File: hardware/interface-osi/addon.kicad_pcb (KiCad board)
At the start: 2 copper layers, 43.2 x 54 mm, 22 parts, among them J1 Conn_01x16, U1 4066, U2 74LS14

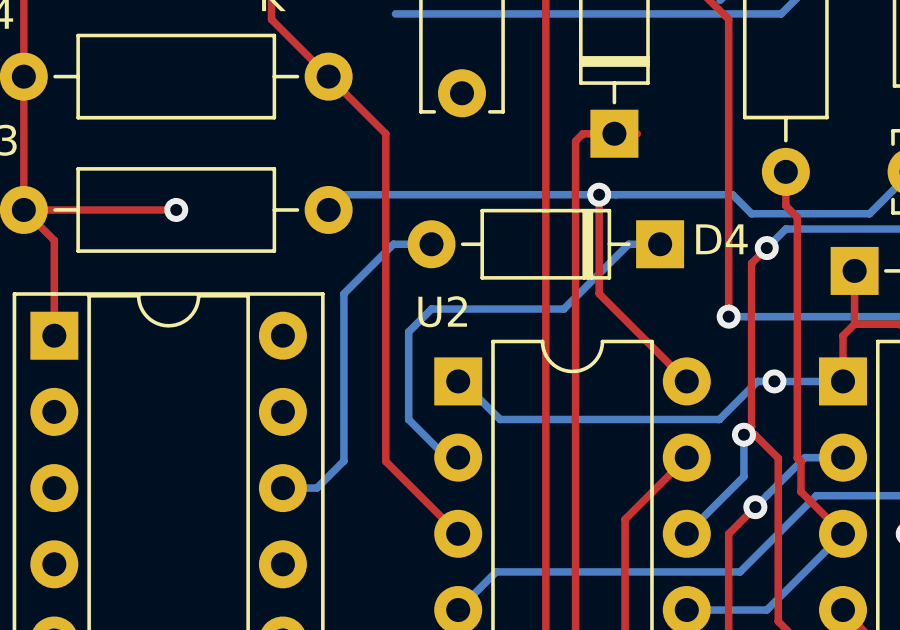
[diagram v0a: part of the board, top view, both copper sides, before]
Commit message: addon board uses 74HC14
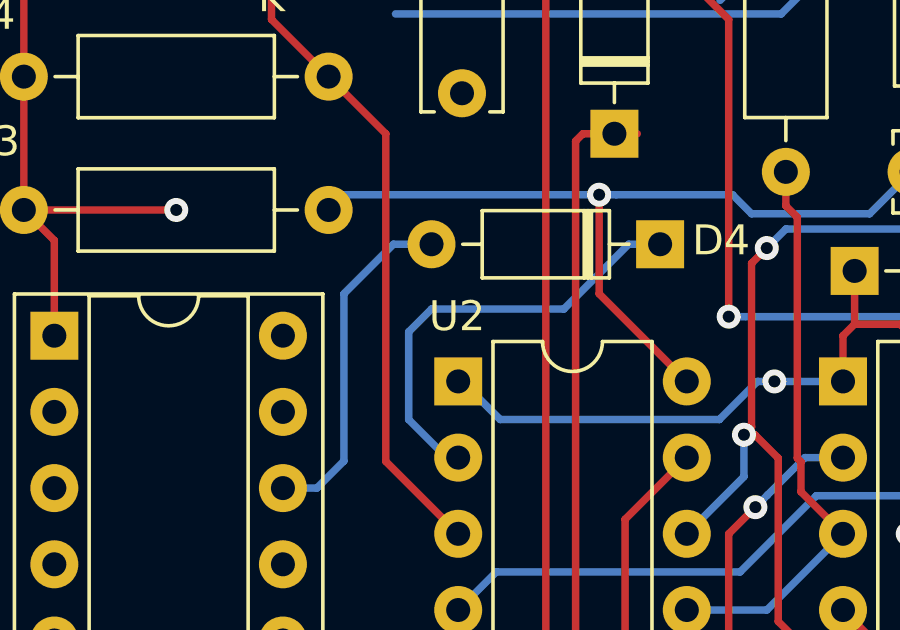
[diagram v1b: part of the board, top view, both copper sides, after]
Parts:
- R5: value 22k -> 10k
- R6: value 220k -> 100k
- U2: value 74LS14 -> 74HC14
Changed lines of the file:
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@@
     (add_net ~RESET)
+  )
+  (module Package_DIP:DIP-14_W7.62mm (layer F.Cu)
+    (at 124.333 62.865)
+    (descr "14-lead though-hole mounted DIP package, row spacing 7.62 mm (300 mils)")
+    (tags "THT DIP DIL PDIP 2.54mm 7.62mm 300mil")
+    (fp_text reference U2 (at -0.0381 -2.1717) (layer F.SilkS)
+      (effects (font (size 1 1) (thickness 0.15)))
+    )
+    (fp_text value 74HC14 (at 3.81 17.57) (layer F.Fab)
+      (effects (font (size 1 1) (thickness 0.15)))
+    )
+    (fp_text user %R (at 3.81 7.62) (layer F.Fab)
+      (effects (font (size 1 1) (thickness 0.15)))
+    )
+    (fp_line (start 8.7 -1.55) (end -1.1 -1.55) (layer F.CrtYd) (width 0.05))
+    (fp_line (start 8.7 16.8) (end 8.7 -1.55) (layer F.CrtYd) (width 0.05))
+    (fp_line (start -1.1 16.8) (end 8.7 16.8) (layer F.CrtYd) (width 0.05))
+    (fp_line (start -1.1 -1.55) (end -1.1 16.8) (layer F.CrtYd) (width 0.05))
+    (fp_line (start 6.46 -1.33) (end 4.81 -1.33) (layer F.SilkS) (width 0.12))
+    (fp_line (start 6.46 16.57) (end 6.46 -1.33) (layer F.SilkS) (width 0.12))
+    (fp_line (start 1.16 16.57) (end 6.46 16.57) (layer F.SilkS) (width 0.12))
+    (fp_line (start 1.16 -1.33) (end 1.16 16.57) (layer F.SilkS) (width 0.12))
+    (fp_line (start 2.81 -1.33) (end 1.16 -1.33) (layer F.SilkS) (width 0.12))
+    (fp_line (start 0.635 -0.27) (end 1.635 -1.27) (layer F.Fab) (width 0.1))
+    (fp_line (start 0.635 16.51) (end 0.635 -0.27) (layer F.Fab) (width 0.1))
+    (fp_line (start 6.985 16.51) (end 0.635 16.51) (layer F.Fab) (width 0.1))
+    (fp_line (start 6.985 -1.27) (end 6.985 16.51) (layer F.Fab) (width 0.1))
+    (fp_line (start 1.635 -1.27) (end 6.985 -1.27) (layer F.Fab) (width 0.1))
+    (fp_arc (start 3.81 -1.33) (end 2.81 -1.33) (angle -180) (layer F.SilkS) (width 0.12))
+    (pad 14 thru_hole oval (at 7.62 0) (size 1.6 1.6) (drill 0.8) (layers *.Cu *.Mask)
+      (net 7 ShifLockLED+))
+    (pad 7 thru_hole oval (at 0 15.24) (size 1.6 1.6) (drill 0.8) (layers *.Cu *.Mask)
+      (net 1 GND))
+    (pad 13 thru_hole oval (at 7.62 2.54) (size 1.6 1.6) (drill 0.8) (layers *.Cu *.Mask)
+      (net 14 "Net-(C1-Pad2)"))
+    (pad 6 thru_hole oval (at 0 12.7) (size 1.6 1.6) (drill 0.8) (layers *.Cu *.Mask)
+      (net 19 "Net-(R7-Pad2)"))
+    (pad 12 thru_hole oval (at 7.62 5.08) (size 1.6 1.6) (drill 0.8) (layers *.Cu *.Mask)
+      (net 4 "Net-(JP1-Pad3)"))
+    (pad 5 thru_hole oval (at 0 10.16) (size 1.6 1.6) (drill 0.8) (layers *.Cu *.Mask)
+      (net 26 "Net-(U1-Pad13)"))
+    (pad 11 thru_hole oval (at 7.62 7.62) (size 1.6 1.6) (drill 0.8) (layers *.Cu *.Mask)
+      (net 18 "Net-(R5-Pad1)"))
+    (pad 4 thru_hole oval (at 0 7.62) (size 1.6 1.6) (drill 0.8) (layers *.Cu *.Mask)
+      (net 26 "Net-(U1-Pad13)"))
+    (pad 10 thru_hole oval (at 7.62 10.16) (size 1.6 1.6) (drill 0.8) (layers *.Cu *.Mask)
+      (net 24 "Net-(JP1-Pad1)"))
+    (pad 3 thru_hole oval (at 0 5.08) (size 1.6 1.6) (drill 0.8) (layers *.Cu *.Mask)
+      (net 15 "Net-(C2-Pad1)"))
+    (pad 9 thru_hole oval (at 7.62 12.7) (size 1.6 1.6) (drill 0.8) (layers *.Cu *.Mask)
+      (net 24 "Net-(JP1-Pad1)"))
+    (pad 2 thru_hole oval (at 0 2.54) (size 1.6 1.6) (drill 0.8) (layers *.Cu *.Mask)
+      (net 27 "Net-(D4-Pad1)"))
+    (pad 8 thru_hole oval (at 7.62 15.24) (size 1.6 1.6) (drill 0.8) (layers *.Cu *.Mask)
+      (net 25 "Net-(R5-Pad2)"))
+    (pad 1 thru_hole rect (at 0 0) (size 1.6 1.6) (drill 0.8) (layers *.Cu *.Mask)
+      (net 22 "Net-(D3-Pad1)"))
+    (model ${KISYS3DMOD}/Package_DIP.3dshapes/DIP-14_W7.62mm.wrl
+      (at (xyz 0 0 0))
+      (scale (xyz 1 1 1))
+      (rotate (xyz 0 0 0))
+    )
   )
   (module Capacitor_THT:C_Disc_D6.0mm_W2.5mm_P5.00mm (layer F.Cu)
@@
     )
   )
-  (module Package_DIP:DIP-14_W7.62mm (layer F.Cu)
-    (at 124.333 62.865)
-    (descr "14-lead though-hole mounted DIP package, row spacing 7.62 mm (300 mils)")
-    (tags "THT DIP DIL PDIP 2.54mm 7.62mm 300mil")
-    (fp_text reference U2 (at -0.508 -2.286) (layer F.SilkS)
-      (effects (font (size 1 1) (thickness 0.15)))
-    )
-    (fp_text value 74LS14 (at 3.81 17.57) (layer F.Fab)
-      (effects (font (size 1 1) (thickness 0.15)))
-    )
-    (fp_text user %R (at 3.81 7.62) (layer F.Fab)
-      (effects (font (size 1 1) (thickness 0.15)))
-    )
-    (fp_line (start 8.7 -1.55) (end -1.1 -1.55) (layer F.CrtYd) (width 0.05))
-    (fp_line (start 8.7 16.8) (end 8.7 -1.55) (layer F.CrtYd) (width 0.05))
-    (fp_line (start -1.1 16.8) (end 8.7 16.8) (layer F.CrtYd) (width 0.05))
-    (fp_line (start -1.1 -1.55) (end -1.1 16.8) (layer F.CrtYd) (width 0.05))
-    (fp_line (start 6.46 -1.33) (end 4.81 -1.33) (layer F.SilkS) (width 0.12))
-    (fp_line (start 6.46 16.57) (end 6.46 -1.33) (layer F.SilkS) (width 0.12))
-    (fp_line (start 1.16 16.57) (end 6.46 16.57) (layer F.SilkS) (width 0.12))
-    (fp_line (start 1.16 -1.33) (end 1.16 16.57) (layer F.SilkS) (width 0.12))
-    (fp_line (start 2.81 -1.33) (end 1.16 -1.33) (layer F.SilkS) (width 0.12))
-    (fp_line (start 0.635 -0.27) (end 1.635 -1.27) (layer F.Fab) (width 0.1))
-    (fp_line (start 0.635 16.51) (end 0.635 -0.27) (layer F.Fab) (width 0.1))
-    (fp_line (start 6.985 16.51) (end 0.635 16.51) (layer F.Fab) (width 0.1))
-    (fp_line (start 6.985 -1.27) (end 6.985 16.51) (layer F.Fab) (width 0.1))
-    (fp_line (start 1.635 -1.27) (end 6.985 -1.27) (layer F.Fab) (width 0.1))
-    (fp_arc (start 3.81 -1.33) (end 2.81 -1.33) (angle -180) (layer F.SilkS) (width 0.12))
-    (pad 14 thru_hole oval (at 7.62 0) (size 1.6 1.6) (drill 0.8) (layers *.Cu *.Mask)
-      (net 7 ShifLockLED+))
-    (pad 7 thru_hole oval (at 0 15.24) (size 1.6 1.6) (drill 0.8) (layers *.Cu *.Mask)
-      (net 1 GND))
-    (pad 13 thru_hole oval (at 7.62 2.54) (size 1.6 1.6) (drill 0.8) (layers *.Cu *.Mask)
-      (net 14 "Net-(C1-Pad2)"))
-    (pad 6 thru_hole oval (at 0 12.7) (size 1.6 1.6) (drill 0.8) (layers *.Cu *.Mask)
-      (net 19 "Net-(R7-Pad2)"))
-    (pad 12 thru_hole oval (at 7.62 5.08) (size 1.6 1.6) (drill 0.8) (layers *.Cu *.Mask)
-      (net 4 "Net-(JP1-Pad3)"))
-    (pad 5 thru_hole oval (at 0 10.16) (size 1.6 1.6) (drill 0.8) (layers *.Cu *.Mask)
-      (net 26 "Net-(U1-Pad13)"))
-    (pad 11 thru_hole oval (at 7.62 7.62) (size 1.6 1.6) (drill 0.8) (layers *.Cu *.Mask)
-      (net 18 "Net-(R5-Pad1)"))
-    (pad 4 thru_hole oval (at 0 7.62) (size 1.6 1.6) (drill 0.8) (layers *.Cu *.Mask)
-      (net 26 "Net-(U1-Pad13)"))
-    (pad 10 thru_hole oval (at 7.62 10.16) (size 1.6 1.6) (drill 0.8) (layers *.Cu *.Mask)
-      (net 24 "Net-(JP1-Pad1)"))
-    (pad 3 thru_hole oval (at 0 5.08) (size 1.6 1.6) (drill 0.8) (layers *.Cu *.Mask)
-      (net 15 "Net-(C2-Pad1)"))
-    (pad 9 thru_hole oval (at 7.62 12.7) (size 1.6 1.6) (drill 0.8) (layers *.Cu *.Mask)
-      (net 24 "Net-(JP1-Pad1)"))
-    (pad 2 thru_hole oval (at 0 2.54) (size 1.6 1.6) (drill 0.8) (layers *.Cu *.Mask)
-      (net 27 "Net-(D4-Pad1)"))
-    (pad 8 thru_hole oval (at 7.62 15.24) (size 1.6 1.6) (drill 0.8) (layers *.Cu *.Mask)
-      (net 25 "Net-(R5-Pad2)"))
-    (pad 1 thru_hole rect (at 0 0) (size 1.6 1.6) (drill 0.8) (layers *.Cu *.Mask)
-      (net 22 "Net-(D3-Pad1)"))
-    (model ${KISYS3DMOD}/Package_DIP.3dshapes/DIP-14_W7.62mm.wrl
-      (at (xyz 0 0 0))
-      (scale (xyz 1 1 1))
-      (rotate (xyz 0 0 0))
-    )
-  )
   (module Resistor_THT:R_Axial_DIN0207_L6.3mm_D2.5mm_P10.16mm_Horizontal (layer F.Cu)
     (at 137.16 87.63)
@@
       (effects (font (size 1 1) (thickness 0.15)))
     )
-    (fp_text value 220k (at 5.08 2.37) (layer F.Fab)
+    (fp_text value 100k (at 5.08 2.37) (layer F.Fab)
       (effects (font (size 1 1) (thickness 0.15)))
     )
@@
       (effects (font (size 1 1) (thickness 0.15)))
     )
-    (fp_text value 22k (at 5.08 2.37 90) (layer F.Fab)
+    (fp_text value 10k (at 5.08 2.37 90) (layer F.Fab)
       (effects (font (size 1 1) (thickness 0.15)))
     )
@@
     (connect_pads (clearance 0.2032))
     (min_thickness 0.2032)
-    (fill yes (arc_segments 32) (thermal_gap 0.2032) (thermal_bridge_width 0.508))
+    (fill (arc_segments 32) (thermal_gap 0.2032) (thermal_bridge_width 0.508))
     (polygon
       (pts
@@
     (connect_pads (clearance 0.2032))
     (min_thickness 0.2032)
-    (fill yes (arc_segments 32) (thermal_gap 0.2032) (thermal_bridge_width 0.508))
+    (fill (arc_segments 32) (thermal_gap 0.2032) (thermal_bridge_width 0.508))
     (polygon
       (pts

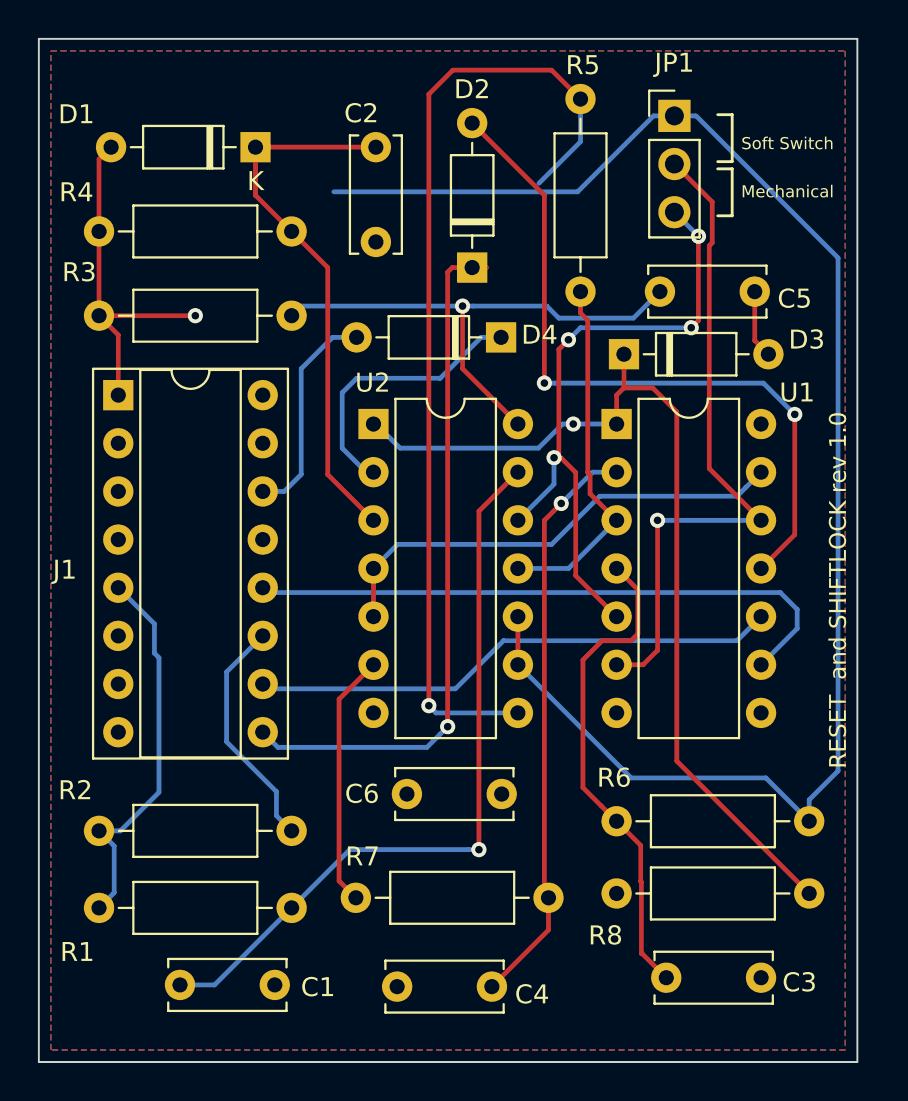
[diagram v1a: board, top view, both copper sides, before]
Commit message: Update addon board updates
- Add diode to C5 to prevent discharge into 5V

- allow selection of default ON or OFF soft switch.
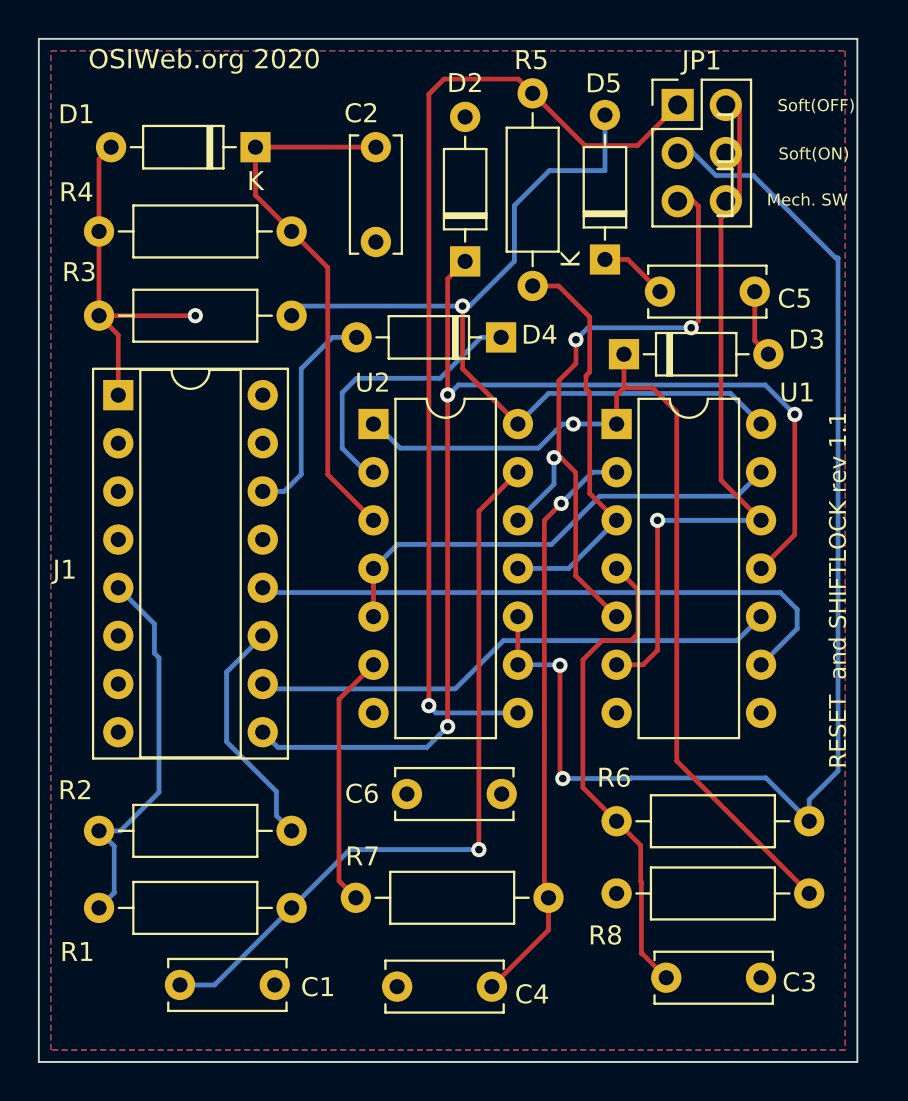
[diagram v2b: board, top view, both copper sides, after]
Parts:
- added D5: 1N914, Diode_THT:D_DO-35_SOD27_P7.62mm_Horizontal, F.Cu at (136.5, 54.2)
- JP1: value Jumper_3_Open -> ShiftLock_Select; footprint Connector_PinHeader_2.54mm:PinHeader_1x03_P2.54mm_Vertical -> Connector_PinHeader_2.54mm:PinHeader_2x03_P2.54mm_Vertical
- moved R5 2.54 mm to (132.7, 55.6)
- moved JP1 0.60 mm to (140.4, 46.0)
- moved D2 0.49 mm to (129.2, 54.3)
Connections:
- C5 pad 1: ShifLockLED+ -> Net-(C5-Pad1)
- R5 pad 2: Net-(R5-Pad2) -> Net-(JP1-Pad1)
- R6 pad 2: Net-(JP1-Pad1) -> Net-(JP1-Pad3)
- U1 pad 11: Net-(D2-Pad2) -> Row0
- U1 pad 5: Net-(JP1-Pad3) -> Net-(JP1-Pad5)
- U2 pad 10: Net-(JP1-Pad1) -> Net-(JP1-Pad3)
- U2 pad 12: Net-(JP1-Pad3) -> Net-(JP1-Pad5)
- U2 pad 8: Net-(R5-Pad2) -> Net-(JP1-Pad1)
- U2 pad 9: Net-(JP1-Pad1) -> Net-(JP1-Pad3)
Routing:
- net Net-(R5-Pad2): track 51.6 -> 0.00 mm, vias 1 -> 0
- net Net-(D2-Pad2): track 38.1 -> 0.00 mm, vias 2 -> 0
- net Net-(JP1-Pad5): track 0.00 -> 34.2 mm, vias 0 -> 3
- net Net-(JP1-Pad3): track 34.1 -> 65.3 mm, vias 4 -> 2
- net Net-(JP1-Pad1): track 83.1 -> 53.1 mm, vias 0 -> 1
- net Row0: track 36.8 -> 63.5 mm, vias 1 -> 3
- net ShifLockLED+: track 40.4 -> 58.4 mm
- net Net-(C5-Pad1): track 0.00 -> 3.60 mm
- net Net-(JP1-Pad2): track 35.6 -> 38.1 mm
- net Net-(R5-Pad1): track 19.1 -> 21.4 mm
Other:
- board text added: "Mech. SW"
- board text added: "OSIWeb.org 2020"
- board text added: "RESET and SHIFTLOCK rev 1.1"
- board text added: "Soft(OFF)"
- board text added: "Soft(ON)"
- board text removed: "Mechanical"
- board text removed: "RESET and SHIFTLOCK rev 1.0"
- board text removed: "Soft Switch"
